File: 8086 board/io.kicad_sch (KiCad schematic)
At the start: 76 parts, among them J2 RM68090, J3 RGB LCD, U22 74AC373, U23 74AC373, U24 74AC373, U25 74AC373, U26 74AC373, U27 74AC373, U28 74AC373, U29 74AC373, U4 74HC02, U5 74HC02

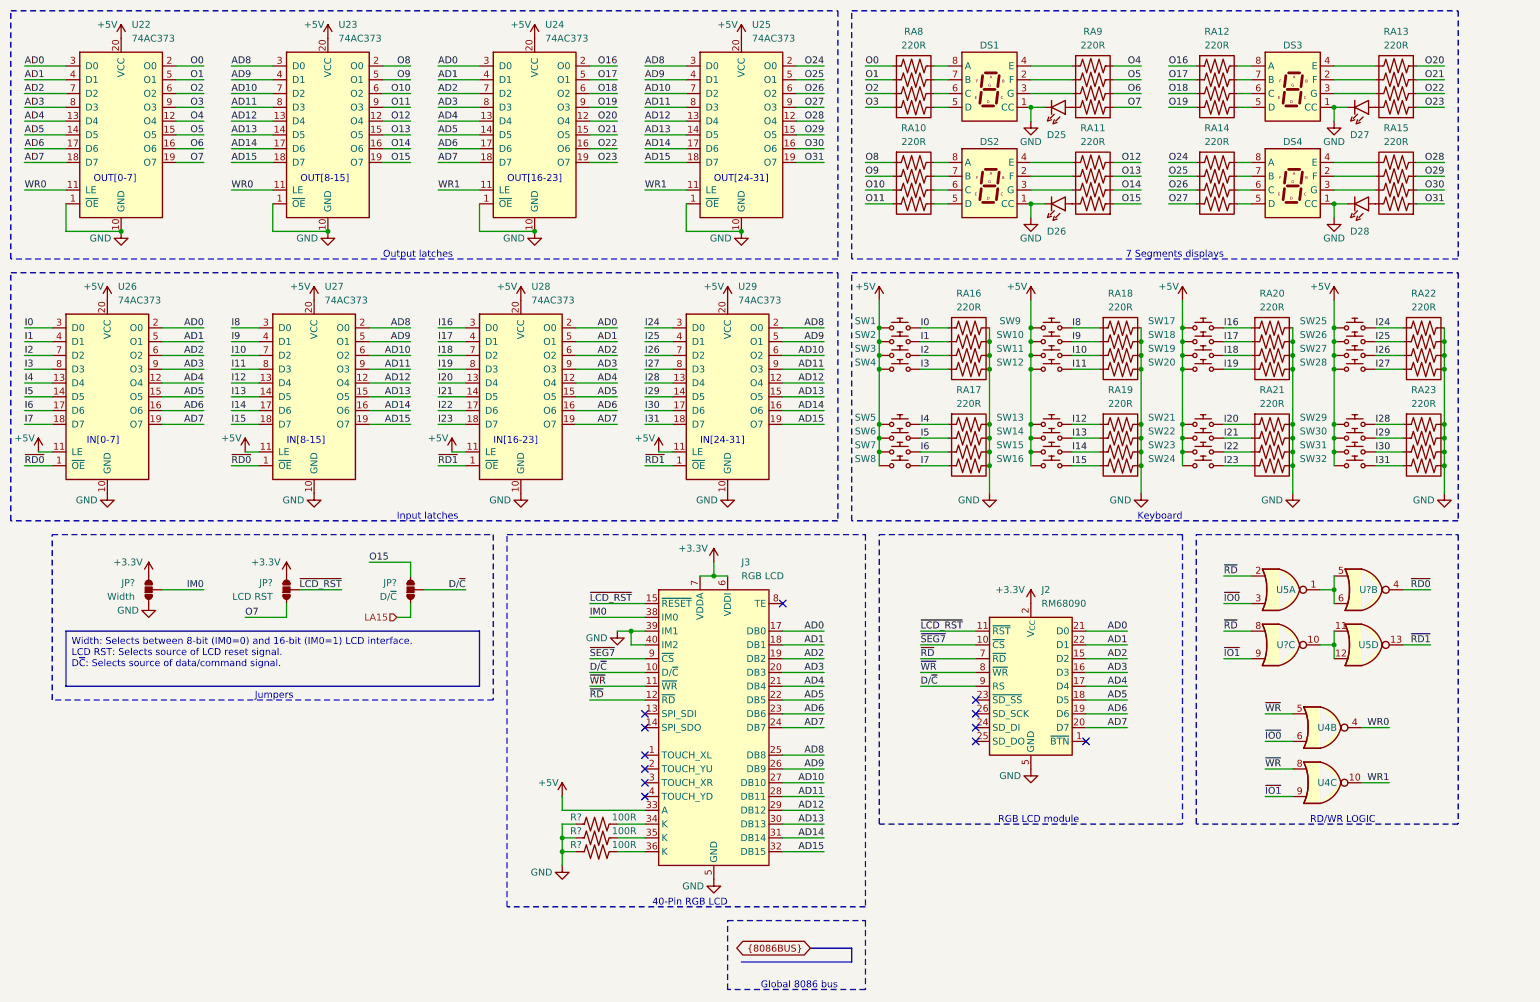
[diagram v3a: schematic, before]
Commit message: -add LCD bus transceiver -add jumper for 7 segments common pin to ground or vcc
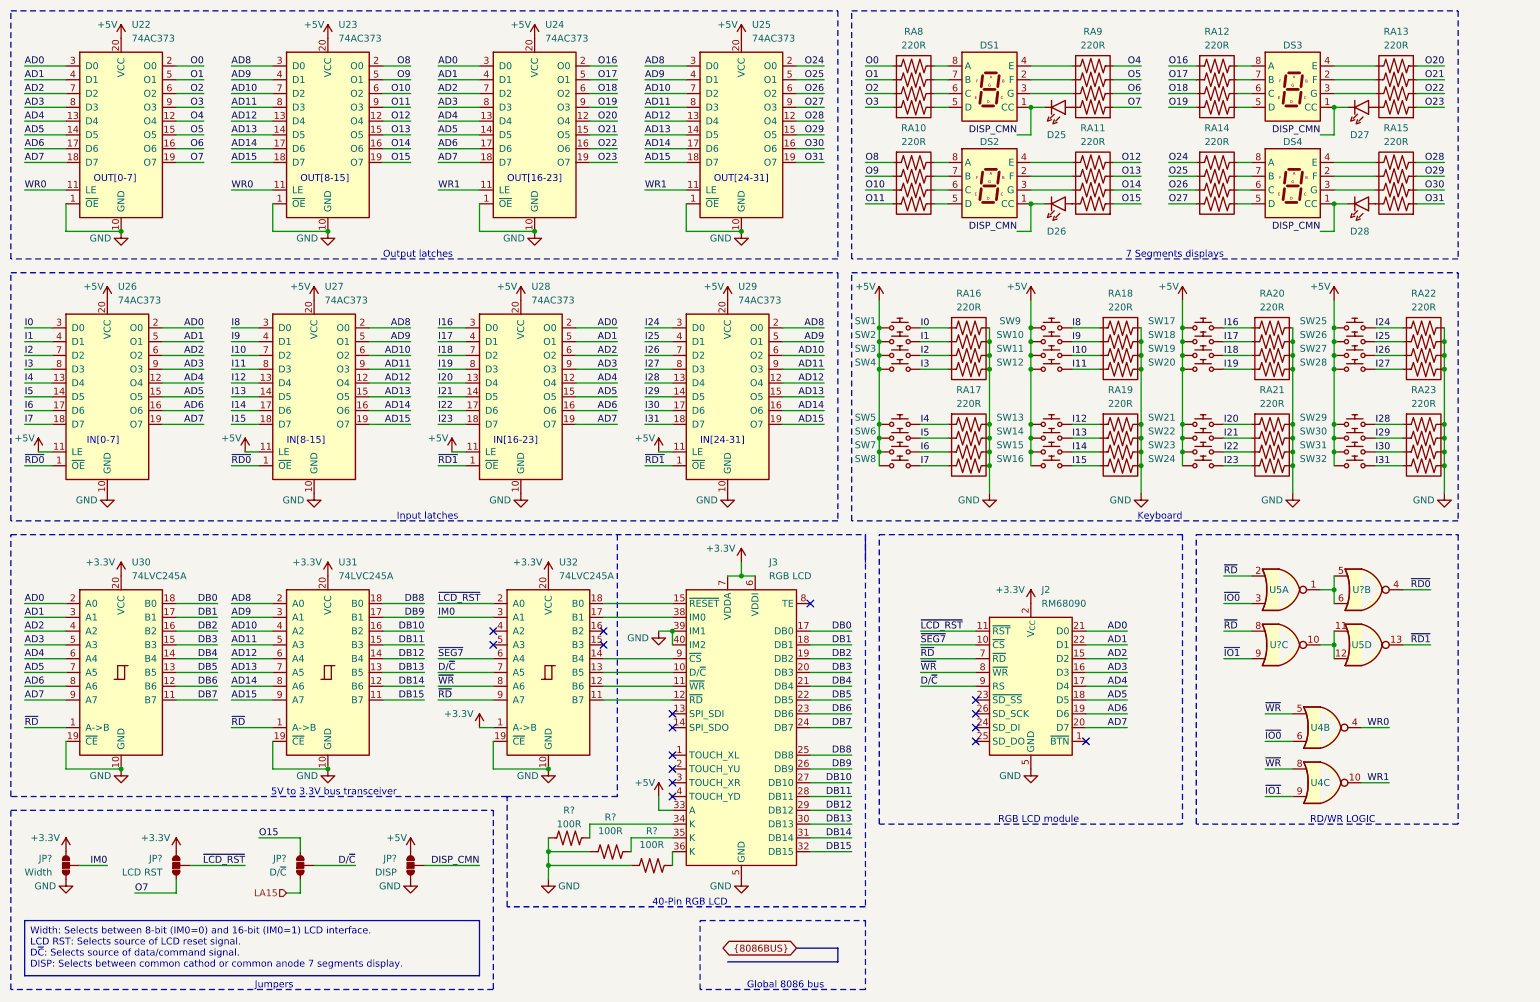
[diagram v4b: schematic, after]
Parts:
- added JP?: DISP, Jumper:SolderJumper-3_P2.0mm_Open_TrianglePad1.0x1.5mm, symbol 8086PC:SolderJumper
- added U30, U31, U32: 74LVC245A, Package_SO:TSSOP-20_4.4x6.5mm_P0.65mm, symbol 8086PC:74LVC245A
- DS1, DS2, DS3, DS4: footprint (none) -> Display_7Segment:KCSC02-105
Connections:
- net +3.3V: now also U30.20 (VCC), U31.20 (VCC), U32.1 (A->B), U32.20 (VCC)
- net +5V: now also JP?.2
- net AD0: now also U30.2 (A0); no longer J3.17 (DB0)
- net AD1: now also U30.3 (A1); no longer J3.18 (DB1)
- net AD10: now also U31.4 (A2); no longer J3.27 (DB10)
- net AD11: now also U31.5 (A3); no longer J3.28 (DB11)
- net AD12: now also U31.6 (A4); no longer J3.29 (DB12)
- net AD13: now also U31.7 (A5); no longer J3.30 (DB13)
- net AD14: now also U31.8 (A6); no longer J3.31 (DB14)
- net AD15: now also U31.9 (A7); no longer J3.32 (DB15)
- net AD2: now also U30.4 (A2); no longer J3.19 (DB2)
- net AD3: now also U30.5 (A3); no longer J3.20 (DB3)
- net AD4: now also U30.6 (A4); no longer J3.21 (DB4)
- net AD5: now also U30.7 (A5); no longer J3.22 (DB5)
- net AD6: now also U30.8 (A6); no longer J3.23 (DB6)
- net AD7: now also U30.9 (A7); no longer J3.24 (DB7)
- net AD8: now also U31.2 (A0); no longer J3.25 (DB8)
- net AD9: now also U31.3 (A1); no longer J3.26 (DB9)
- net D/~{C}: now also U32.7 (A5); no longer J3.10 (D/~{C})
- net GND: now also JP?.1, U30.10 (GND), U30.19 (~{CE}), U31.10 (GND), U31.19 (~{CE}), U32.10 (GND), U32.19 (~{CE}); no longer D25.2 (K), D26.2 (K), D27.2 (K), D28.2 (K), DS1.1 (CC), DS2.1 (CC), DS3.1 (CC), DS4.1 (CC)
- net IM0: now also U32.3 (A1); no longer J3.38 (IM0)
- net ~{LCD_RST}: now also U32.2 (A0); no longer J3.15 (~{RESET})
- net ~{RD}: now also U30.1 (A->B), U31.1 (A->B), U32.9 (A7); no longer J3.12 (~{RD})
- net ~{SEG7}: now also U32.6 (A4); no longer J3.9 (~{CS})
- net ~{WR}: now also U32.8 (A6); no longer J3.11 (~{WR})
- new net: J3.12 (~{RD}), U32.11 (B7)
- new net: J3.11 (~{WR}), U32.12 (B6)
- new net: J3.10 (D/~{C}), U32.13 (B5)
- new net: J3.9 (~{CS}), U32.14 (B4)
- new net: J3.38 (IM0), U32.17 (B1)
- new net: J3.15 (~{RESET}), U32.18 (B0)
- new net DB0: J3.17 (DB0), U30.18 (B0)
- new net DB1: J3.18 (DB1), U30.17 (B1)
- new net DB10: J3.27 (DB10), U31.16 (B2)
- new net DB11: J3.28 (DB11), U31.15 (B3)
- new net DB12: J3.29 (DB12), U31.14 (B4)
- new net DB13: J3.30 (DB13), U31.13 (B5)
- new net DB14: J3.31 (DB14), U31.12 (B6)
- new net DB15: J3.32 (DB15), U31.11 (B7)
- new net DB2: J3.19 (DB2), U30.16 (B2)
- new net DB3: J3.20 (DB3), U30.15 (B3)
- new net DB4: J3.21 (DB4), U30.14 (B4)
- new net DB5: J3.22 (DB5), U30.13 (B5)
- new net DB6: J3.23 (DB6), U30.12 (B6)
- new net DB7: J3.24 (DB7), U30.11 (B7)
- new net DB8: J3.25 (DB8), U31.18 (B0)
- new net DB9: J3.26 (DB9), U31.17 (B1)
- new net DISP_CMN: D25.2 (K), D26.2 (K), D27.2 (K), D28.2 (K), DS1.1 (CC), DS2.1 (CC), DS3.1 (CC), DS4.1 (CC), JP?.3
- no-connect marks 12 -> 16
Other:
- note added: "5V to 3.3V bus transceiver"
- company: (none) -> Eldad Hellerman
- title: (none) -> 8086 computer
- moved on the sheet: J3, JP?, R?

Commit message: change 7 segment to custom symbol and footprint
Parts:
- DS1, DS2, DS3, DS4: footprint Display_7Segment:KCSC02-105 -> 8086PC:2181AS
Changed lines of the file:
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@@
       (effects (font (size 1.27 1.27)) hide)
     )
-    (property "Footprint" "Display_7Segment:KCSC02-105" (at 195.58 30.48 0)
+    (property "Footprint" "8086PC:2181AS" (at 195.58 30.48 0)
       (effects (font (size 1.27 1.27)) hide)
     )
@@
       (effects (font (size 1.27 1.27)) hide)
     )
-    (property "Footprint" "Display_7Segment:KCSC02-105" (at 195.58 48.26 0)
+    (property "Footprint" "8086PC:2181AS" (at 195.58 48.26 0)
       (effects (font (size 1.27 1.27)) hide)
     )
@@
       (effects (font (size 1.27 1.27)) hide)
     )
-    (property "Footprint" "Display_7Segment:KCSC02-105" (at 251.46 48.26 0)
+    (property "Footprint" "8086PC:2181AS" (at 251.46 48.26 0)
       (effects (font (size 1.27 1.27)) hide)
     )
@@
       (effects (font (size 1.27 1.27)) hide)
     )
-    (property "Footprint" "Display_7Segment:KCSC02-105" (at 251.46 30.48 0)
-      (effects (font (size 1.27 1.27)) hide)
-    )
+    (property "Footprint" "8086PC:2181AS" (at 251.46 30.48 0)
+      (effects (font (size 1.27 1.27)) hide)
+    )

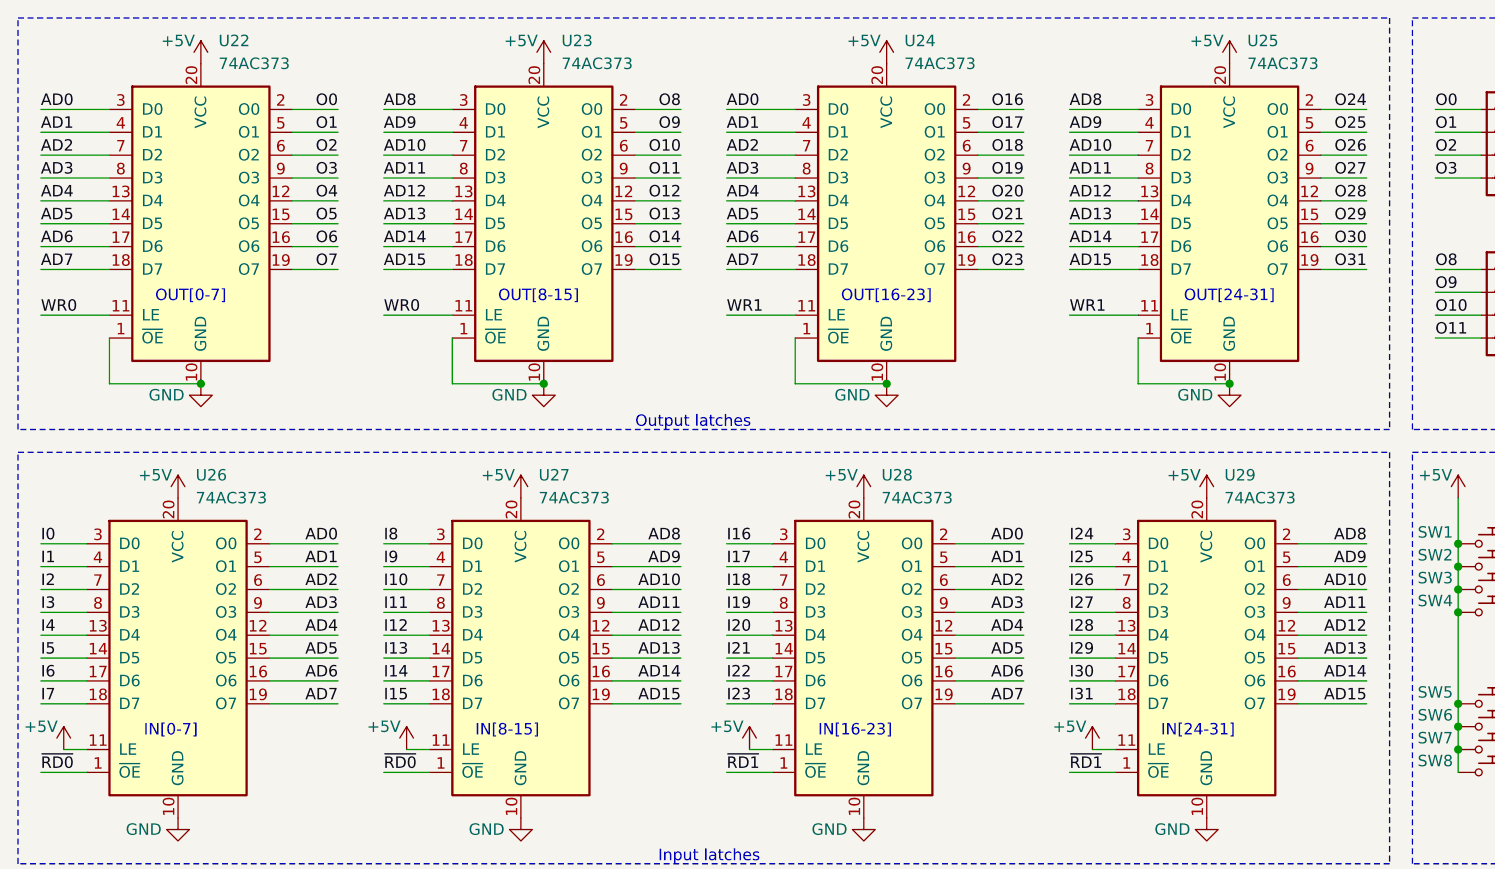
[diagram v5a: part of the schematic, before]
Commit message: change 74HC373D (SO20) to 74HC573PW (TSSOP20)
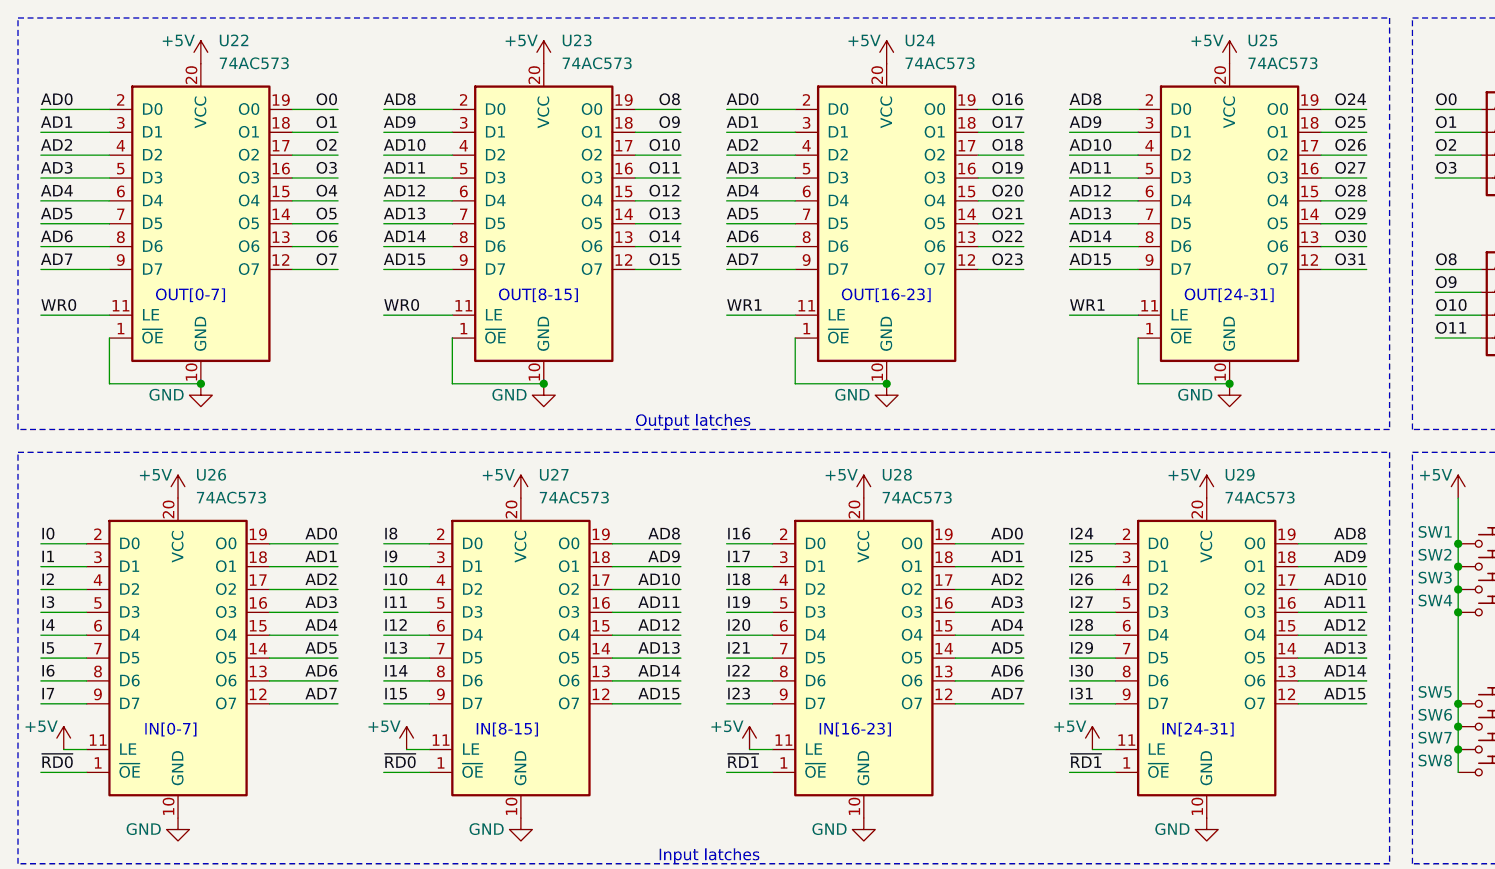
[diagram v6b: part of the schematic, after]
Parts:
- removed U22, U23, U24, U25, U26, U27, U28: 74AC373, Package_SO:SOIC-20W_7.5x12.8mm_P1.27mm, symbol 8086PC:74AC373
- removed U29: 74AC373, Package_SO:TSSOP-20_4.4x6.5mm_P0.65mm, symbol 8086PC:74AC373
- added U22, U23, U24, U25, U26, U27, U28, U29: 74AC573, Package_SO:TSSOP-20_4.4x6.5mm_P0.65mm, symbol 8086PC:74AC573
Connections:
- net +5V: now also U22.20 (VCC), U23.20 (VCC), U24.20 (VCC), U25.20 (VCC), U26.11 (LE), U26.20 (VCC), U27.11 (LE), U27.20 (VCC), U28.11 (LE), U28.20 (VCC), U29.11 (LE), U29.20 (VCC)
- net AD0: now also U22.2 (D0), U24.2 (D0), U26.19 (O0), U28.19 (O0)
- net AD1: now also U22.3 (D1), U24.3 (D1), U26.18 (O1), U28.18 (O1)
- net AD10: now also U23.4 (D2), U25.4 (D2), U27.17 (O2), U29.17 (O2)
- net AD11: now also U23.5 (D3), U25.5 (D3), U27.16 (O3), U29.16 (O3)
- net AD12: now also U23.6 (D4), U25.6 (D4), U27.15 (O4), U29.15 (O4)
- net AD13: now also U23.7 (D5), U25.7 (D5), U27.14 (O5), U29.14 (O5)
- net AD14: now also U23.8 (D6), U25.8 (D6), U27.13 (O6), U29.13 (O6)
- net AD15: now also U23.9 (D7), U25.9 (D7), U27.12 (O7), U29.12 (O7)
- net AD2: now also U22.4 (D2), U24.4 (D2), U26.17 (O2), U28.17 (O2)
- net AD3: now also U22.5 (D3), U24.5 (D3), U26.16 (O3), U28.16 (O3)
- net AD4: now also U22.6 (D4), U24.6 (D4), U26.15 (O4), U28.15 (O4)
- net AD5: now also U22.7 (D5), U24.7 (D5), U26.14 (O5), U28.14 (O5)
- net AD6: now also U22.8 (D6), U24.8 (D6), U26.13 (O6), U28.13 (O6)
- net AD7: now also U22.9 (D7), U24.9 (D7), U26.12 (O7), U28.12 (O7)
- net AD8: now also U23.2 (D0), U25.2 (D0), U27.19 (O0), U29.19 (O0)
- net AD9: now also U23.3 (D1), U25.3 (D1), U27.18 (O1), U29.18 (O1)
- net GND: now also U22.1 (~{OE}), U22.10 (GND), U23.1 (~{OE}), U23.10 (GND), U24.1 (~{OE}), U24.10 (GND), U25.1 (~{OE}), U25.10 (GND), U26.10 (GND), U27.10 (GND), U28.10 (GND), U29.10 (GND)
- net I0: now also U26.2 (D0)
- net I1: now also U26.3 (D1)
- net I10: now also U27.4 (D2)
- net I11: now also U27.5 (D3)
- net I12: now also U27.6 (D4)
- net I13: now also U27.7 (D5)
- net I14: now also U27.8 (D6)
- net I15: now also U27.9 (D7)
- net I16: now also U28.2 (D0)
- net I17: now also U28.3 (D1)
- net I18: now also U28.4 (D2)
- net I19: now also U28.5 (D3)
- net I2: now also U26.4 (D2)
- net I20: now also U28.6 (D4)
- net I21: now also U28.7 (D5)
- net I22: now also U28.8 (D6)
- net I23: now also U28.9 (D7)
- net I24: now also U29.2 (D0)
- net I25: now also U29.3 (D1)
- net I26: now also U29.4 (D2)
- net I27: now also U29.5 (D3)
- net I28: now also U29.6 (D4)
- net I29: now also U29.7 (D5)
- net I3: now also U26.5 (D3)
- net I30: now also U29.8 (D6)
- net I31: now also U29.9 (D7)
- net I4: now also U26.6 (D4)
- net I5: now also U26.7 (D5)
- net I6: now also U26.8 (D6)
- net I7: now also U26.9 (D7)
- net I8: now also U27.2 (D0)
- net I9: now also U27.3 (D1)
- net O0: now also U22.19 (O0)
- net O1: now also U22.18 (O1)
- net O10: now also U23.17 (O2)
- net O11: now also U23.16 (O3)
- net O12: now also U23.15 (O4)
- net O13: now also U23.14 (O5)
- net O14: now also U23.13 (O6)
- net O15: now also U23.12 (O7)
- net O16: now also U24.19 (O0)
- net O17: now also U24.18 (O1)
- net O18: now also U24.17 (O2)
- net O19: now also U24.16 (O3)
- net O2: now also U22.17 (O2)
- net O20: now also U24.15 (O4)
- net O21: now also U24.14 (O5)
- net O22: now also U24.13 (O6)
- net O23: now also U24.12 (O7)
- net O24: now also U25.19 (O0)
- net O25: now also U25.18 (O1)
- net O26: now also U25.17 (O2)
- net O27: now also U25.16 (O3)
- net O28: now also U25.15 (O4)
- net O29: now also U25.14 (O5)
- net O3: now also U22.16 (O3)
- net O30: now also U25.13 (O6)
- net O31: now also U25.12 (O7)
- net O4: now also U22.15 (O4)
- net O5: now also U22.14 (O5)
- net O6: now also U22.13 (O6)
- net O7: now also U22.12 (O7)
- net O8: now also U23.19 (O0)
- net O9: now also U23.18 (O1)
- net WR0: now also U22.11 (LE), U23.11 (LE)
- net WR1: now also U24.11 (LE), U25.11 (LE)
- net ~{RD0}: now also U26.1 (~{OE}), U27.1 (~{OE})
- net ~{RD1}: now also U28.1 (~{OE}), U29.1 (~{OE})
